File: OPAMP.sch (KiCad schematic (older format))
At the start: 21 parts

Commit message: Stand 10.03
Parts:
- added P? (x3): CONN_01X02, symbol CONN_01X02
- R? (x4): value 1M -> 110k
- R? (x4): value 7.5k -> 10k
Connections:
- net V_in_1 is gone; now on net +3V3: R?.1
- net GND: now also P?.1 (P1), P?.1 (P1), P?.1 (P1)
- net V_in_2: now also P?.2 (P2)
- net V_in_3: now also P?.2 (P2)
- net V_in_4: now also P?.2 (P2)
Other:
- moved on the sheet: C?, R?, U?A

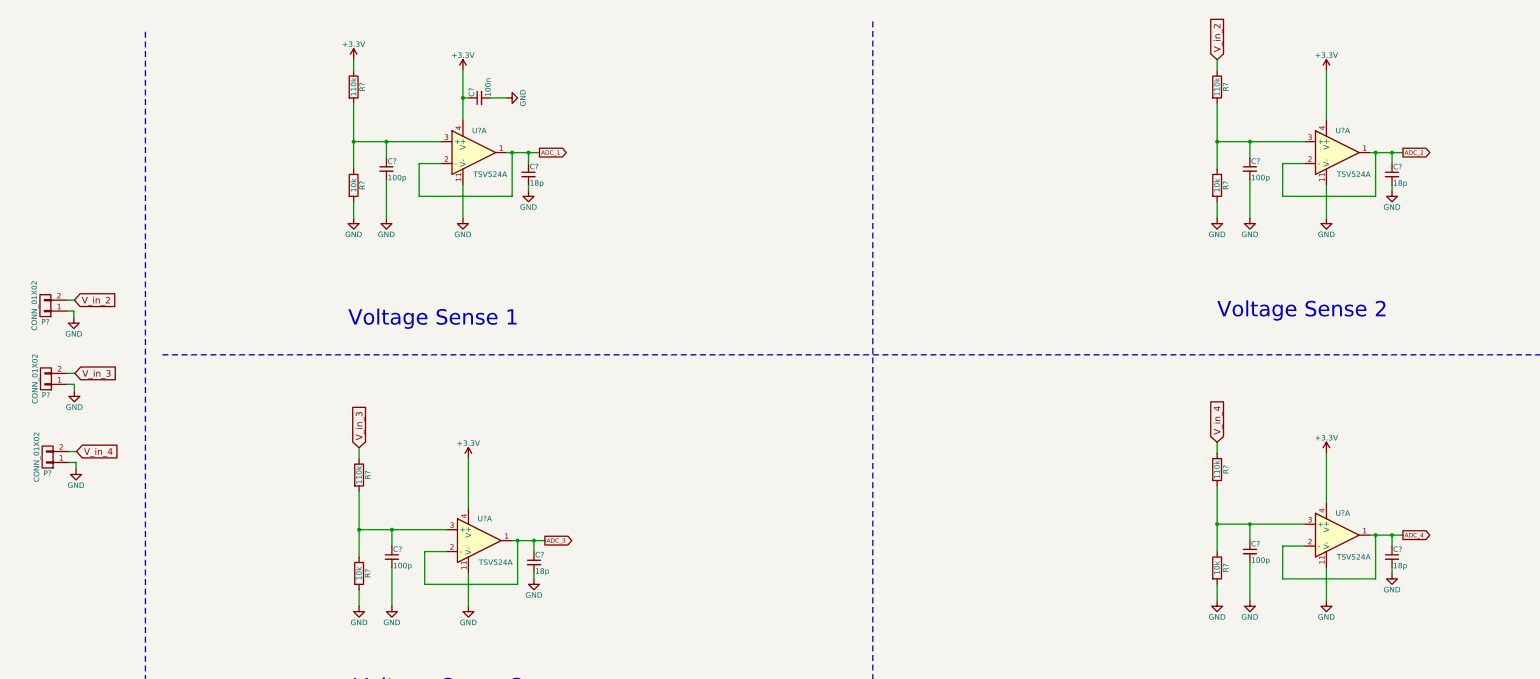
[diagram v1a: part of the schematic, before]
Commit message: schematics ==> Check (exept BW) Layout started
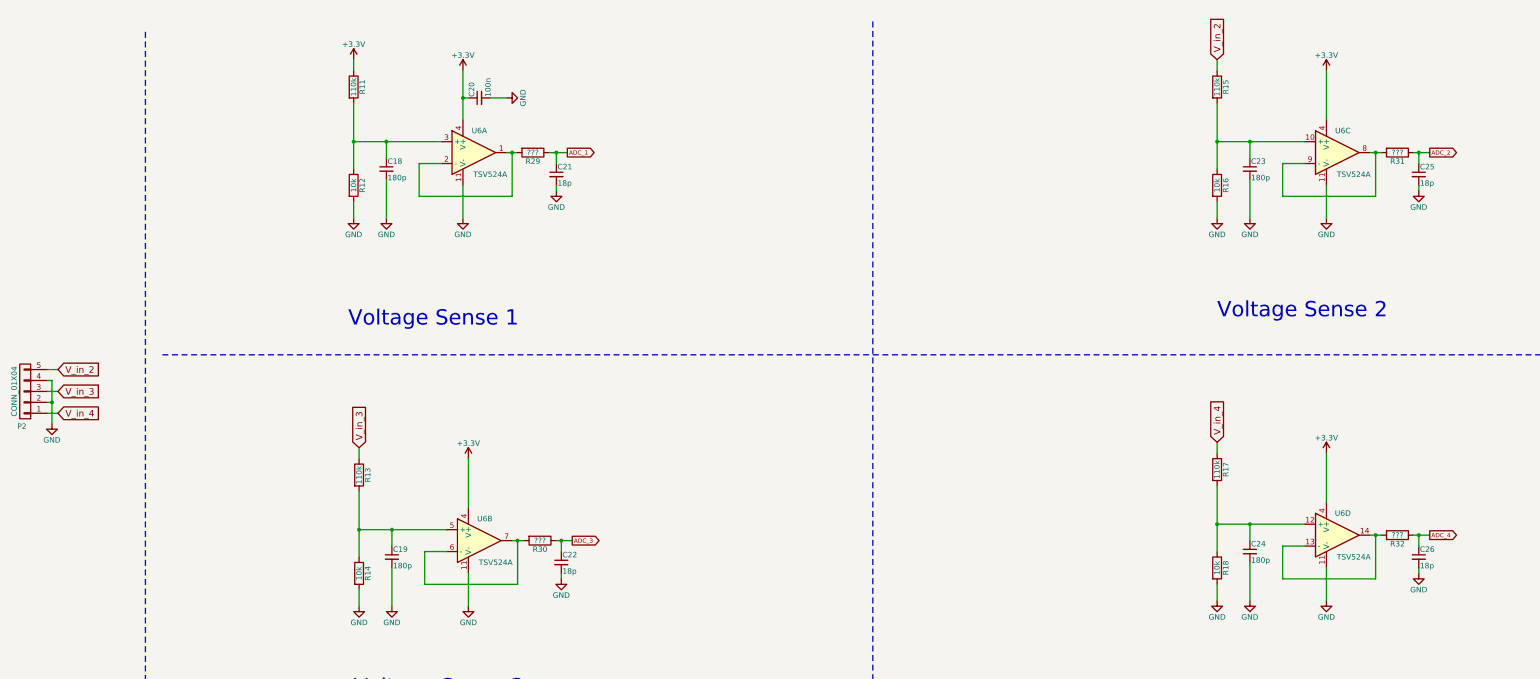
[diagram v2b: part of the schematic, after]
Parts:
- removed P? (x3): CONN_01X02, symbol CONN_01X02
- added P2: CONN_01X04, Connectors_Molex:Molex_KK-6410-05_05x2.54mm_Straight, symbol CONN_01X05
- added R29, R30, R31, R32: ???, Resistors_SMD:R_0603, symbol R
- C18, C19, C23, C24: renamed from C?; value 100p -> 180p
- R11, R13, R15, R17: renamed from R?; footprint Resistors_SMD:R_1206 -> Resistors_SMD:R_0603
- gave numbers to parts that had none: 10
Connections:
- net ADC_1: now also R29.1; no longer U6.1, U6.2 (-)
- net ADC_2: now also R31.1; no longer U6.1, U6.2 (-)
- net ADC_3: now also R30.1; no longer U6.1, U6.2 (-)
- net ADC_4: now also R32.1; no longer U6.1, U6.2 (-)
- net GND: now also P2.2 (P2), P2.4 (P4)
- net V_in_2: now also P2.5 (P5)
- net V_in_3: now also P2.3 (P3)
- net V_in_4: now also P2.1 (P1)
- net at C23.1, R15.2, R16.1: now also U6.10 (+); no longer U6.3 (+)
- net at C19.1, R13.2, R14.1: now also U6.5 (+); no longer U6.3 (+)
- net at C24.1, R17.2, R18.1: now also U6.12 (+); no longer U6.3 (+)
- new net: R29.2, U6.1, U6.2 (-)
- new net: R31.2, U6.8, U6.9 (-)
- new net: R30.2, U6.6 (-), U6.7
- new net: R32.2, U6.13 (-), U6.14
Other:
- moved on the sheet: C21, C22, C25, C26

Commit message: All parts in places (exept :Leds)
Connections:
- net V_in_2: now also P2.3 (P3); no longer P2.5 (P5)
- net V_in_3: now also P2.1 (P1); no longer P2.3 (P3)
- net V_in_4: now also P2.5 (P5); no longer P2.1 (P1)
- net OpAmp_Out2: now reaches R31.2, U6.8, U6.9 (-)
- net OpAmp_Out4: now reaches R32.2, U6.13 (-), U6.14
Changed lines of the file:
@@
 	1    0    0    -1
 $EndComp
-Wire Wire Line
-	4030 2010 4030 2610
-Wire Wire Line
-	4030 2910 4030 3060
-Wire Wire Line
-	4330 2710 4330 3060
-Wire Wire Line
-	4030 1710 4030 1610
 Text GLabel 5985 2460 2    39   Output ~ 0
 ADC_1
@@
 	0    -1   -1   0
 $EndComp
-Connection ~ 5030 1960
-Wire Wire Line
-	5280 1960 5430 1960
-Wire Wire Line
-	5030 2760 5030 3060
 $Comp
 L MCP6004 U6
@@
 	1    0    0    -1
 $EndComp
-Wire Wire Line
-	4330 2510 4330 2360
-Wire Wire Line
-	5080 1960 5030 1960
-Wire Wire Line
-	4830 2560 4630 2560
-Wire Wire Line
-	4630 2560 4630 2860
-Wire Wire Line
-	4630 2860 5480 2860
-Wire Wire Line
-	5480 2860 5480 2460
-Wire Wire Line
-	5030 1710 5030 2160
-Wire Wire Line
-	4030 2360 4830 2360
-Connection ~ 4030 2360
-Connection ~ 4330 2360
 $Comp
 L +3.3V #PWR022
@@
 	1    0    0    -1
 $EndComp
-Wire Wire Line
-	5885 2560 5885 2460
-Connection ~ 5885 2460
 $Comp
 L GND #PWR027
@@
 	1    0    0    -1
 $EndComp
-Wire Wire Line
-	5885 2760 5885 2810
 Text Notes 3980 4060 0    140  ~ 0
 Voltage Sense 1\n
@@
 	1    0    0    -1
 $EndComp
-Wire Wire Line
-	11930 2010 11930 2610
-Wire Wire Line
-	11930 2910 11930 3060
-Wire Wire Line
-	12230 2710 12230 3060
 Text GLabel 11930 1610 1    60   Input ~ 0
 V_in_2
-Wire Wire Line
-	11930 1710 11930 1610
 Text GLabel 13875 2460 2    39   Output ~ 0
 ADC_2
-Wire Wire Line
-	12930 2760 12930 3060
 $Comp
 L MCP6004 U6
@@
 	1    0    0    -1
 $EndComp
-Wire Wire Line
-	12230 2510 12230 2360
-Wire Wire Line
-	13330 2460 13430 2460
-Wire Wire Line
-	13730 2460 13875 2460
-Wire Wire Line
-	12730 2560 12530 2560
-Wire Wire Line
-	12530 2560 12530 2860
-Wire Wire Line
-	12530 2860 13380 2860
-Wire Wire Line
-	13380 2860 13380 2460
-Connection ~ 13380 2460
-Wire Wire Line
-	12930 1710 12930 2160
-Wire Wire Line
-	11930 2360 12730 2360
-Connection ~ 11930 2360
-Connection ~ 12230 2360
 $Comp
 L +3.3V #PWR028
@@
 	1    0    0    -1
 $EndComp
-Wire Wire Line
-	13775 2560 13775 2460
-Connection ~ 13775 2460
 $Comp
 L GND #PWR032
@@
 	1    0    0    -1
 $EndComp
-Wire Wire Line
-	13775 2760 13775 2810
 Text Notes 11930 4210 0    140  ~ 0
 Voltage Sense 2\n\n
@@
 	1    0    0    -1
 $EndComp
-Wire Wire Line
-	4080 5560 4080 6160
-Wire Wire Line
-	4080 6460 4080 6610
-Wire Wire Line
-	4380 6260 4380 6610
 Text GLabel 4080 5160 1    60   Input ~ 0
 V_in_3
-Wire Wire Line
-	4080 5260 4080 5160
 Text GLabel 6030 6010 2    39   Output ~ 0
 ADC_3
-Wire Wire Line
-	5080 6310 5080 6610
 $Comp
 L MCP6004 U6
@@
 	1    0    0    -1
 $EndComp
-Wire Wire Line
-	4380 6060 4380 5910
-Wire Wire Line
-	5480 6010 5585 6010
-Wire Wire Line
-	4880 6110 4680 6110
-Wire Wire Line
-	4680 6110 4680 6410
-Wire Wire Line
-	4680 6410 5530 6410
-Wire Wire Line
-	5530 6410 5530 6010
-Connection ~ 5530 6010
-Wire Wire Line
-	5080 5260 5080 5710
-Wire Wire Line
-	4080 5910 4880 5910
-Connection ~ 4080 5910
-Connection ~ 4380 5910
 $Comp
 L +3.3V #PWR033
@@
 	1    0    0    -1
 $EndComp
-Wire Wire Line
-	5930 6310 5930 6360
 Text Notes 4030 7660 0    140  ~ 0
 Voltage Sense 3\n\n
@@
 	1    0    0    -1
 $EndComp
-Wire Wire Line
-	11930 5510 11930 6110
-Wire Wire Line
-	11930 6410 11930 6560
-Wire Wire Line
-	12230 6210 12230 6560
 Text GLabel 11930 5110 1    60   Input ~ 0
 V_in_4
-Wire Wire Line
-	11930 5210 11930 5110
 Text GLabel 13875 5960 2    39   Output ~ 0
 ADC_4
-Wire Wire Line
-	12930 6260 12930 6560
 $Comp
 L MCP6004 U6
@@
 	1    0    0    -1
 $EndComp
-Wire Wire Line
-	12230 6010 12230 5860
-Wire Wire Line
-	13330 5960 13430 5960
-Wire Wire Line
-	13730 5960 13875 5960
-Wire Wire Line
-	12730 6060 12530 6060
-Wire Wire Line
-	12530 6060 12530 6360
-Wire Wire Line
-	12530 6360 13380 6360
-Wire Wire Line
-	13380 6360 13380 5960
-Connection ~ 13380 5960
-Wire Wire Line
-	12930 5210 12930 5660
-Wire Wire Line
-	11930 5860 12730 5860
-Connection ~ 11930 5860
-Connection ~ 12230 5860
 $Comp
 L +3.3V #PWR038
@@
 	1    0    0    -1
 $EndComp
-Wire Wire Line
-	13775 6060 13775 5960
-Connection ~ 13775 5960
 $Comp
 L GND #PWR042
@@
 	1    0    0    -1
 $EndComp
-Wire Wire Line
-	13775 6260 13775 6310
 Text Notes 12080 7560 0    140  ~ 0
 Voltage Sense 4\n
-Wire Notes Line
-	8780 1260 8780 7510
-Wire Notes Line
-	2280 4310 15830 4310
 Text Notes 7360 945  0    180  ~ 0
 Voltage Sense
 Text Notes 3015 8970 0    100  ~ 0
 Hier noch 1 von den EIngängen mit Vin (vin kann bis 40V hochgehen) und (vielleicht eins noch mit 3.3V verbinden, die restlichen mit connectoren verbinden
-Text GLabel 1325 4445 2    60   Input ~ 0
+Text GLabel 1330 4445 2    60   Input ~ 0
+V_in_4
+Text GLabel 1325 4645 2    60   Input ~ 0
 V_in_2
-Wire Notes Line
-	2125 1355 2125 7490
-Wire Notes Line
-	2125 7490 2145 7490
-Text GLabel 1325 4645 2    60   Input ~ 0
+Text GLabel 1325 4845 2    60   Input ~ 0
 V_in_3
-Text GLabel 1325 4845 2    60   Input ~ 0
-V_in_4
 $Comp
 L +3.3V #PWR043
@@
 	-1   0    0    1
 $EndComp
-Wire Wire Line
-	1330 4445 1225 4445
-Wire Wire Line
-	1325 4645 1225 4645
-Wire Wire Line
-	1325 4845 1225 4845
-Wire Wire Line
-	1225 4745 1270 4745
-Wire Wire Line
-	1225 4545 1270 4545
 $Comp
 L GND #PWR044
@@
 	1    0    0    -1
 $EndComp
-Wire Wire Line
-	1270 4545 1270 4940
-Connection ~ 1270 4745
 $Comp
 L R R29
@@
 	0    1    1    0
 $EndComp
-Wire Wire Line
-	5430 2460 5520 2460
-Connection ~ 5480 2460
-Wire Wire Line
-	5820 2460 5985 2460
 $Comp
 L R R31
@@
 	0    1    1    0
 $EndComp
+Text GLabel 13380 2320 1    60   Input ~ 0
+OpAmp_Out2
+Wire Wire Line
+	4030 2010 4030 2610
+Wire Wire Line
+	4030 2910 4030 3060
+Wire Wire Line
+	4330 2710 4330 3060
+Wire Wire Line
+	4030 1710 4030 1610
+Connection ~ 5030 1960
+Wire Wire Line
+	5280 1960 5430 1960
+Wire Wire Line
+	5030 2760 5030 3060
+Wire Wire Line
+	4330 2510 4330 2360
+Wire Wire Line
+	5080 1960 5030 1960
+Wire Wire Line
+	4830 2560 4630 2560
+Wire Wire Line
+	4630 2560 4630 2860
+Wire Wire Line
+	4630 2860 5480 2860
+Wire Wire Line
+	5480 2860 5480 2460
+Wire Wire Line
+	5030 1710 5030 2160
+Wire Wire Line
+	4030 2360 4830 2360
+Connection ~ 4030 2360
+Connection ~ 4330 2360
+Wire Wire Line
+	5885 2560 5885 2460
+Connection ~ 5885 2460
+Wire Wire Line
+	5885 2760 5885 2810
+Wire Wire Line
+	11930 2010 11930 2610
+Wire Wire Line
+	11930 2910 11930 3060
+Wire Wire Line
+	12230 2710 12230 3060
+Wire Wire Line
+	11930 1710 11930 1610
+Wire Wire Line
+	12930 2760 12930 3060
+Wire Wire Line
+	12230 2510 12230 2360
+Wire Wire Line
+	13330 2460 13430 2460
+Wire Wire Line
+	13730 2460 13875 2460
+Wire Wire Line
+	12730 2560 12530 2560
+Wire Wire Line
+	12530 2560 12530 2860
+Wire Wire Line
+	13380 2860 12530 2860
+Wire Wire Line
+	13380 2320 13380 2860
+Connection ~ 13380 2460
+Wire Wire Line
+	12930 1710 12930 2160
+Wire Wire Line
+	11930 2360 12730 2360
+Connection ~ 11930 2360
+Connection ~ 12230 2360
+Wire Wire Line
+	13775 2560 13775 2460
+Connection ~ 13775 2460
+Wire Wire Line
+	13775 2760 13775 2810
+Wire Wire Line
+	4080 5560 4080 6160
+Wire Wire Line
+	4080 6460 4080 6610
+Wire Wire Line
+	4380 6260 4380 6610
+Wire Wire Line
+	4080 5260 4080 5160
+Wire Wire Line
+	5080 6310 5080 6610
+Wire Wire Line
+	4380 6060 4380 5910
+Wire Wire Line
+	5480 6010 5585 6010
+Wire Wire Line
+	4880 6110 4680 6110
+Wire Wire Line
+	4680 6110 4680 6410
+Wire Wire Line
+	4680 6410 5530 6410
+Wire Wire Line
+	5530 6410 5530 6010
+Connection ~ 5530 6010
+Wire Wire Line
+	5080 5260 5080 5710
+Wire Wire Line
+	4080 5910 4880 5910
+Connection ~ 4080 5910
+Connection ~ 4380 5910
+Wire Wire Line
+	5930 6310 5930 6360
+Wire Wire Line
+	11930 5510 11930 6110
+Wire Wire Line
+	11930 6410 11930 6560
+Wire Wire Line
+	12230 6210 12230 6560
+Wire Wire Line
+	11930 5210 11930 5110
+Wire Wire Line
+	12930 6260 12930 6560
+Wire Wire Line
+	12230 6010 12230 5860
+Wire Wire Line
+	13330 5960 13430 5960
+Wire Wire Line
+	13730 5960 13875 5960
+Wire Wire Line
+	12730 6060 12530 6060
+Wire Wire Line
+	12530 6060 12530 6360
+Wire Wire Line
+	13380 6360 12530 6360
+Wire Wire Line
+	13380 5825 13380 6360
+Connection ~ 13380 5960
+Wire Wire Line
+	12930 5210 12930 5660
+Wire Wire Line
+	11930 5860 12730 5860
+Connection ~ 11930 5860
+Connection ~ 12230 5860
+Wire Wire Line
+	13775 6060 13775 5960
+Connection ~ 13775 5960
+Wire Wire Line
+	13775 6260 13775 6310
+Wire Notes Line
+	8780 1260 8780 7510
+Wire Notes Line
+	2280 4310 15830 4310
+Wire Notes Line
+	2125 1355 2125 7490
+Wire Notes Line
+	2125 7490 2145 7490
+Wire Wire Line
+	1330 4445 1225 4445
+Wire Wire Line
+	1325 4645 1225 4645
+Wire Wire Line
+	1325 4845 1225 4845
+Wire Wire Line
+	1225 4745 1270 4745
+Wire Wire Line
+	1225 4545 1270 4545
+Wire Wire Line
+	1270 4545 1270 4940
+Connection ~ 1270 4745
+Wire Wire Line
+	5430 2460 5520 2460
+Connection ~ 5480 2460
+Wire Wire Line
+	5820 2460 5985 2460
 Wire Wire Line
 	5885 6010 6030 6010
@@
 	5930 6110 5930 6010
 Connection ~ 5930 6010
+Text GLabel 13380 5825 1    60   Input ~ 0
+OpAmp_Out4
 $EndSCHEMATC

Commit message: Started with tracking
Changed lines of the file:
@@
 	12530 2560 12530 2860
 Wire Wire Line
-	13380 2860 12530 2860
+	12530 2860 13380 2860
 Wire Wire Line
-	13380 2320 13380 2860
+	13380 2860 13380 2320
 Connection ~ 13380 2460
 Wire Wire Line
@@
 	12530 6060 12530 6360
 Wire Wire Line
-	13380 6360 12530 6360
+	12530 6360 13380 6360
 Wire Wire Line
-	13380 5825 13380 6360
+	13380 6360 13380 5825
 Connection ~ 13380 5960
 Wire Wire Line

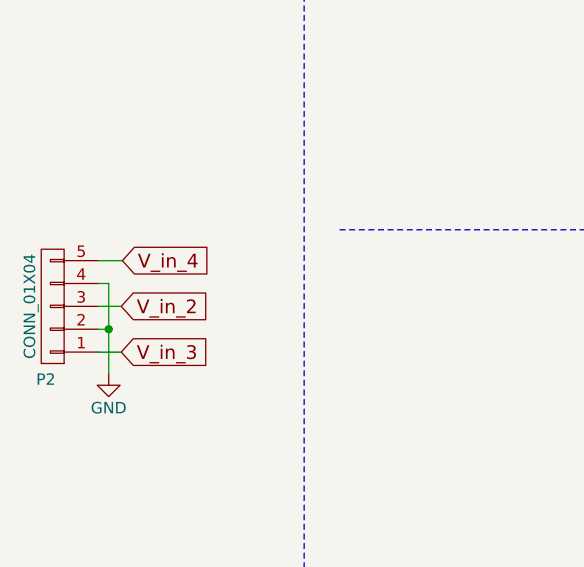
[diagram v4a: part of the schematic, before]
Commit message: added missing parts (SPI conn / Boost Conn/ drills..)
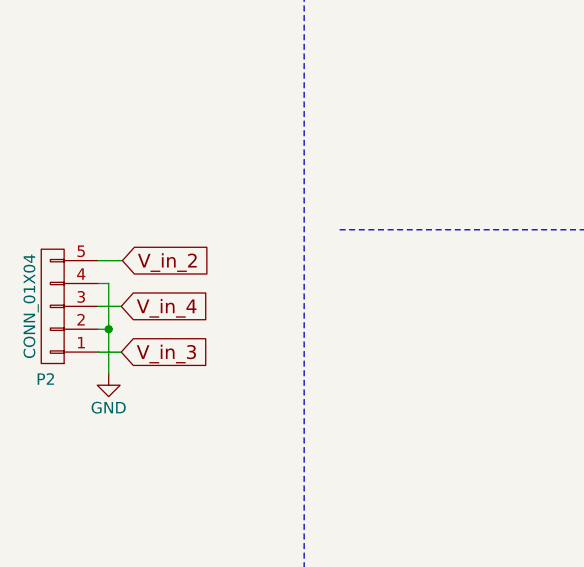
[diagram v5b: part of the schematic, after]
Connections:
- net V_in_2: now also P2.5 (P5); no longer P2.3 (P3)
- net V_in_4: now also P2.3 (P3); no longer P2.5 (P5)
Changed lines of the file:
@@
 $EndComp
 $Comp
-L +3.3V #PWR022
+L +3.3V #PWR29
 U 1 1 58BDE975
 P 5030 1710
-F 0 "#PWR022" H 5030 1560 50  0001 C CNN
+F 0 "#PWR29" H 5030 1560 50  0001 C CNN
 F 1 "+3.3V" H 5030 1850 50  0000 C CNN
 F 2 "" H 5030 1710 50  0000 C CNN
@@
 $EndComp
 $Comp
-L GND #PWR023
+L GND #PWR30
 U 1 1 58BDE976
 P 5030 3060
-F 0 "#PWR023" H 5030 2810 50  0001 C CNN
+F 0 "#PWR30" H 5030 2810 50  0001 C CNN
 F 1 "GND" H 5030 2910 50  0000 C CNN
 F 2 "" H 5030 3060 50  0000 C CNN
@@
 $EndComp
 $Comp
-L GND #PWR024
+L GND #PWR27
 U 1 1 58BDE977
 P 4330 3060
-F 0 "#PWR024" H 4330 2810 50  0001 C CNN
+F 0 "#PWR27" H 4330 2810 50  0001 C CNN
 F 1 "GND" H 4330 2910 50  0000 C CNN
 F 2 "" H 4330 3060 50  0000 C CNN
@@
 $EndComp
 $Comp
-L GND #PWR025
+L GND #PWR25
 U 1 1 58BDE978
 P 4030 3060
-F 0 "#PWR025" H 4030 2810 50  0001 C CNN
+F 0 "#PWR25" H 4030 2810 50  0001 C CNN
 F 1 "GND" H 4030 2910 50  0000 C CNN
 F 2 "" H 4030 3060 50  0000 C CNN
@@
 $EndComp
 $Comp
-L GND #PWR026
+L GND #PWR33
 U 1 1 58BDE979
 P 5430 1960
-F 0 "#PWR026" H 5430 1710 50  0001 C CNN
+F 0 "#PWR33" H 5430 1710 50  0001 C CNN
 F 1 "GND" H 5430 1810 50  0000 C CNN
 F 2 "" H 5430 1960 50  0000 C CNN
@@
 $EndComp
 $Comp
-L GND #PWR027
+L GND #PWR34
 U 1 1 58BDE97B
 P 5885 2810
-F 0 "#PWR027" H 5885 2560 50  0001 C CNN
+F 0 "#PWR34" H 5885 2560 50  0001 C CNN
 F 1 "GND" H 5885 2660 50  0000 C CNN
 F 2 "" H 5885 2810 50  0000 C CNN
@@
 $EndComp
 $Comp
-L +3.3V #PWR028
+L +3.3V #PWR40
 U 1 1 58BDE980
 P 12930 1710
-F 0 "#PWR028" H 12930 1560 50  0001 C CNN
+F 0 "#PWR40" H 12930 1560 50  0001 C CNN
 F 1 "+3.3V" H 12930 1850 50  0000 C CNN
 F 2 "" H 12930 1710 50  0000 C CNN
@@
 $EndComp
 $Comp
-L GND #PWR029
+L GND #PWR41
 U 1 1 58BDE981
 P 12930 3060
-F 0 "#PWR029" H 12930 2810 50  0001 C CNN
+F 0 "#PWR41" H 12930 2810 50  0001 C CNN
 F 1 "GND" H 12930 2910 50  0000 C CNN
 F 2 "" H 12930 3060 50  0000 C CNN
@@
 $EndComp
 $Comp
-L GND #PWR030
+L GND #PWR38
 U 1 1 58BDE982
 P 12230 3060
-F 0 "#PWR030" H 12230 2810 50  0001 C CNN
+F 0 "#PWR38" H 12230 2810 50  0001 C CNN
 F 1 "GND" H 12230 2910 50  0000 C CNN
 F 2 "" H 12230 3060 50  0000 C CNN
@@
 $EndComp
 $Comp
-L GND #PWR031
+L GND #PWR36
 U 1 1 58BDE983
 P 11930 3060
-F 0 "#PWR031" H 11930 2810 50  0001 C CNN
+F 0 "#PWR36" H 11930 2810 50  0001 C CNN
 F 1 "GND" H 11930 2910 50  0000 C CNN
 F 2 "" H 11930 3060 50  0000 C CNN
@@
 $EndComp
 $Comp
-L GND #PWR032
+L GND #PWR44
 U 1 1 58BDE985
 P 13775 2810
-F 0 "#PWR032" H 13775 2560 50  0001 C CNN
+F 0 "#PWR44" H 13775 2560 50  0001 C CNN
 F 1 "GND" H 13775 2660 50  0000 C CNN
 F 2 "" H 13775 2810 50  0000 C CNN
@@
 $EndComp
 $Comp
-L +3.3V #PWR033
+L +3.3V #PWR31
 U 1 1 58BDE98A
 P 5080 5260
-F 0 "#PWR033" H 5080 5110 50  0001 C CNN
+F 0 "#PWR31" H 5080 5110 50  0001 C CNN
 F 1 "+3.3V" H 5080 5400 50  0000 C CNN
 F 2 "" H 5080 5260 50  0000 C CNN
@@
 $EndComp
 $Comp
-L GND #PWR034
+L GND #PWR32
 U 1 1 58BDE98B
 P 5080 6610
-F 0 "#PWR034" H 5080 6360 50  0001 C CNN
+F 0 "#PWR32" H 5080 6360 50  0001 C CNN
 F 1 "GND" H 5080 6460 50  0000 C CNN
 F 2 "" H 5080 6610 50  0000 C CNN
@@
 $EndComp
 $Comp
-L GND #PWR035
+L GND #PWR28
 U 1 1 58BDE98C
 P 4380 6610
-F 0 "#PWR035" H 4380 6360 50  0001 C CNN
+F 0 "#PWR28" H 4380 6360 50  0001 C CNN
 F 1 "GND" H 4380 6460 50  0000 C CNN
 F 2 "" H 4380 6610 50  0000 C CNN
@@
 $EndComp
 $Comp
-L GND #PWR036
+L GND #PWR26
 U 1 1 58BDE98D
 P 4080 6610
-F 0 "#PWR036" H 4080 6360 50  0001 C CNN
+F 0 "#PWR26" H 4080 6360 50  0001 C CNN
 F 1 "GND" H 4080 6460 50  0000 C CNN
 F 2 "" H 4080 6610 50  0000 C CNN
@@
 $EndComp
 $Comp
-L GND #PWR037
+L GND #PWR35
 U 1 1 58BDE98F
 P 5930 6360
-F 0 "#PWR037" H 5930 6110 50  0001 C CNN
+F 0 "#PWR35" H 5930 6110 50  0001 C CNN
 F 1 "GND" H 5930 6210 50  0000 C CNN
 F 2 "" H 5930 6360 50  0000 C CNN
@@
 $EndComp
 $Comp
-L +3.3V #PWR038
+L +3.3V #PWR42
 U 1 1 58BDE994
 P 12930 5210
-F 0 "#PWR038" H 12930 5060 50  0001 C CNN
+F 0 "#PWR42" H 12930 5060 50  0001 C CNN
 F 1 "+3.3V" H 12930 5350 50  0000 C CNN
 F 2 "" H 12930 5210 50  0000 C CNN
@@
 $EndComp
 $Comp
-L GND #PWR039
+L GND #PWR43
 U 1 1 58BDE995
 P 12930 6560
-F 0 "#PWR039" H 12930 6310 50  0001 C CNN
+F 0 "#PWR43" H 12930 6310 50  0001 C CNN
 F 1 "GND" H 12930 6410 50  0000 C CNN
 F 2 "" H 12930 6560 50  0000 C CNN
@@
 $EndComp
 $Comp
-L GND #PWR040
+L GND #PWR39
 U 1 1 58BDE996
 P 12230 6560
-F 0 "#PWR040" H 12230 6310 50  0001 C CNN
+F 0 "#PWR39" H 12230 6310 50  0001 C CNN
 F 1 "GND" H 12230 6410 50  0000 C CNN
 F 2 "" H 12230 6560 50  0000 C CNN
@@
 $EndComp
 $Comp
-L GND #PWR041
+L GND #PWR37
 U 1 1 58BDE997
 P 11930 6560
-F 0 "#PWR041" H 11930 6310 50  0001 C CNN
+F 0 "#PWR37" H 11930 6310 50  0001 C CNN
 F 1 "GND" H 11930 6410 50  0000 C CNN
 F 2 "" H 11930 6560 50  0000 C CNN
@@
 $EndComp
 $Comp
-L GND #PWR042
+L GND #PWR45
 U 1 1 58BDE999
 P 13775 6310
-F 0 "#PWR042" H 13775 6060 50  0001 C CNN
+F 0 "#PWR45" H 13775 6060 50  0001 C CNN
 F 1 "GND" H 13775 6160 50  0000 C CNN
 F 2 "" H 13775 6310 50  0000 C CNN
@@
 Hier noch 1 von den EIngängen mit Vin (vin kann bis 40V hochgehen) und (vielleicht eins noch mit 3.3V verbinden, die restlichen mit connectoren verbinden
 Text GLabel 1330 4445 2    60   Input ~ 0
+V_in_2
+Text GLabel 1325 4645 2    60   Input ~ 0
 V_in_4
-Text GLabel 1325 4645 2    60   Input ~ 0
-V_in_2
 Text GLabel 1325 4845 2    60   Input ~ 0
 V_in_3
 $Comp
-L +3.3V #PWR043
+L +3.3V #PWR24
 U 1 1 58C3E0DE
 P 4030 1610
-F 0 "#PWR043" H 4030 1460 50  0001 C CNN
+F 0 "#PWR24" H 4030 1460 50  0001 C CNN
 F 1 "+3.3V" H 4030 1750 50  0000 C CNN
 F 2 "" H 4030 1610 50  0000 C CNN
@@
 $EndComp
 $Comp
-L GND #PWR044
+L GND #PWR23
 U 1 1 58C7F1E0
 P 1270 4940
-F 0 "#PWR044" H 1270 4690 50  0001 C CNN
+F 0 "#PWR23" H 1270 4690 50  0001 C CNN
 F 1 "GND" H 1270 4790 50  0000 C CNN
 F 2 "" H 1270 4940 50  0000 C CNN
